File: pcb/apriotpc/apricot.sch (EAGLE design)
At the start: 16 parts, among them J2 ATX24RH

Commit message: added grounding blade and exposed screw pad, added psw blade
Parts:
- added U$5, U$6: M3_MOUNTING_HOLE, apricot:M3_MOUNTING_HOLE
- added U$7: 6MM_BLADE, apricot:6MM_BLADE
- JP1: device pinhead:PINHD-1X2/90 -> pinhead:PINHD-1X2
- U$1, U$3: value M3_MOUNTING_HOLE -> 6MM_BLADE; device a:M3_MOUNTING_HOLE -> apricot:6MM_BLADE
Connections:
- net GND: now also JP1.1, U$3.P$1, U$3.P$2, U$5.P$1, U$5.P$2, U$6.P$1, U$6.P$2, U$7.P$1, U$7.P$2; no longer JP1.2
- net N$1: now also JP1.2, U$1.P$1, U$1.P$2; no longer JP1.1
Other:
- moved on the sheet: JP1
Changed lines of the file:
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@@
 <part name="GND4" library="supply1" library_urn="urn:adsk.eagle:library:371" deviceset="GND" device=""/>
 <part name="JP3" library="appleii" deviceset="4PIN_FAN" device=""/>
-<part name="U$1" library="a" deviceset="M3_MOUNTING_HOLE" device=""/>
-<part name="U$3" library="a" deviceset="M3_MOUNTING_HOLE" device=""/>
 <part name="GND1" library="supply1" library_urn="urn:adsk.eagle:library:371" deviceset="GND" device=""/>
 <part name="C2" library="capacitor-wima" library_urn="urn:adsk.eagle:library:116" deviceset="C" device="5/2.5" package3d_urn="urn:adsk.eagle:package:5426/1"/>
@@
 <part name="GND9" library="supply1" library_urn="urn:adsk.eagle:library:371" deviceset="GND" device=""/>
 <part name="U$4" library="396_conn" deviceset="VH396" device=""/>
-<part name="JP1" library="pinhead" library_urn="urn:adsk.eagle:library:325" deviceset="PINHD-1X2" device="/90" package3d_urn="urn:adsk.eagle:package:22437/2"/>
+<part name="JP1" library="pinhead" library_urn="urn:adsk.eagle:library:325" deviceset="PINHD-1X2" device="" package3d_urn="urn:adsk.eagle:package:22435/2"/>
 <part name="P+1" library="supply1" library_urn="urn:adsk.eagle:library:371" deviceset="+12V" device=""/>
 <part name="P+4" library="supply1" library_urn="urn:adsk.eagle:library:371" deviceset="+5V" device=""/>
@@
 <part name="GND13" library="supply1" library_urn="urn:adsk.eagle:library:371" deviceset="GND" device=""/>
 <part name="P+13" library="supply1" library_urn="urn:adsk.eagle:library:371" deviceset="+5V" device=""/>
+<part name="U$5" library="apricot" deviceset="M3_MOUNTING_HOLE" device=""/>
+<part name="U$6" library="apricot" deviceset="M3_MOUNTING_HOLE" device=""/>
+<part name="GND6" library="supply1" library_urn="urn:adsk.eagle:library:371" deviceset="GND" device=""/>
+<part name="U$1" library="apricot" deviceset="6MM_BLADE" device=""/>
+<part name="U$3" library="apricot" deviceset="6MM_BLADE" device=""/>
+<part name="U$7" library="apricot" deviceset="6MM_BLADE" device=""/>
+<part name="GND14" library="supply1" library_urn="urn:adsk.eagle:library:371" deviceset="GND" device=""/>
 </parts>
 <sheets>
@@
 </instance>
 <instance part="JP3" gate="A" x="-55.88" y="132.08" smashed="yes"/>
-<instance part="U$1" gate="G$1" x="-66.04" y="170.18" smashed="yes"/>
-<instance part="U$3" gate="G$1" x="-66.04" y="160.02" smashed="yes"/>
-<instance part="GND1" gate="1" x="121.92" y="154.94" smashed="yes">
-<attribute name="VALUE" x="119.38" y="152.4" size="1.778" layer="96"/>
+<instance part="GND1" gate="1" x="139.7" y="162.56" smashed="yes">
+<attribute name="VALUE" x="137.16" y="160.02" size="1.778" layer="96"/>
 </instance>
 <instance part="C2" gate="G$1" x="152.4" y="149.86" smashed="yes">
@@
 </instance>
 <instance part="U$4" gate="G$1" x="27.94" y="132.08" smashed="yes" rot="R180"/>
-<instance part="JP1" gate="G$1" x="132.08" y="160.02" smashed="yes">
-<attribute name="NAME" x="125.73" y="165.735" size="1.778" layer="95"/>
-<attribute name="VALUE" x="125.73" y="154.94" size="1.778" layer="96"/>
+<instance part="JP1" gate="G$1" x="132.08" y="162.56" smashed="yes">
+<attribute name="NAME" x="125.73" y="168.275" size="1.778" layer="95"/>
+<attribute name="VALUE" x="125.73" y="157.48" size="1.778" layer="96"/>
 </instance>
 <instance part="P+1" gate="1" x="43.18" y="142.24" smashed="yes" rot="MR0">
@@
 <instance part="P+13" gate="1" x="71.12" y="101.6" smashed="yes">
 <attribute name="VALUE" x="68.58" y="96.52" size="1.778" layer="96" rot="R90"/>
+</instance>
+<instance part="U$5" gate="G$1" x="-35.56" y="187.96" smashed="yes"/>
+<instance part="U$6" gate="G$1" x="-35.56" y="170.18" smashed="yes"/>
+<instance part="GND6" gate="1" x="-7.62" y="165.1" smashed="yes">
+<attribute name="VALUE" x="-10.16" y="162.56" size="1.778" layer="96"/>
+</instance>
+<instance part="U$1" gate="G$1" x="127" y="132.08" smashed="yes" rot="R90"/>
+<instance part="U$3" gate="G$1" x="190.5" y="119.38" smashed="yes"/>
+<instance part="U$7" gate="G$1" x="190.5" y="129.54" smashed="yes"/>
+<instance part="GND14" gate="1" x="218.44" y="114.3" smashed="yes">
+<attribute name="VALUE" x="215.9" y="111.76" size="1.778" layer="96"/>
 </instance>
 </instances>
@@
 </segment>
 <segment>
-<pinref part="JP1" gate="G$1" pin="2"/>
-<pinref part="GND1" gate="1" pin="GND"/>
-<wire x1="129.54" y1="160.02" x2="121.92" y2="160.02" width="0.1524" layer="91"/>
-<wire x1="121.92" y1="160.02" x2="121.92" y2="157.48" width="0.1524" layer="91"/>
-</segment>
-<segment>
 <pinref part="U$4" gate="G$1" pin="P$2"/>
 <pinref part="GND3" gate="1" pin="GND"/>
@@
 <pinref part="C8" gate="G$1" pin="2"/>
 <pinref part="GND13" gate="1" pin="GND"/>
+</segment>
+<segment>
+<pinref part="U$5" gate="G$1" pin="P$1"/>
+<pinref part="GND6" gate="1" pin="GND"/>
+<wire x1="-12.7" y1="193.04" x2="-7.62" y2="193.04" width="0.1524" layer="91"/>
+<wire x1="-7.62" y1="193.04" x2="-7.62" y2="185.42" width="0.1524" layer="91"/>
+<pinref part="U$5" gate="G$1" pin="P$2"/>
+<wire x1="-7.62" y1="185.42" x2="-7.62" y2="175.26" width="0.1524" layer="91"/>
+<wire x1="-7.62" y1="175.26" x2="-7.62" y2="167.64" width="0.1524" layer="91"/>
+<wire x1="-12.7" y1="185.42" x2="-7.62" y2="185.42" width="0.1524" layer="91"/>
+<junction x="-7.62" y="185.42"/>
+<pinref part="U$6" gate="G$1" pin="P$1"/>
+<wire x1="-12.7" y1="175.26" x2="-7.62" y2="175.26" width="0.1524" layer="91"/>
+<junction x="-7.62" y="175.26"/>
+<pinref part="U$6" gate="G$1" pin="P$2"/>
+<wire x1="-12.7" y1="167.64" x2="-7.62" y2="167.64" width="0.1524" layer="91"/>
+<junction x="-7.62" y="167.64"/>
+</segment>
+<segment>
+<pinref part="JP1" gate="G$1" pin="1"/>
+<pinref part="GND1" gate="1" pin="GND"/>
+<wire x1="129.54" y1="165.1" x2="139.7" y2="165.1" width="0.1524" layer="91"/>
+</segment>
+<segment>
+<pinref part="U$7" gate="G$1" pin="P$1"/>
+<pinref part="GND14" gate="1" pin="GND"/>
+<wire x1="208.28" y1="132.08" x2="218.44" y2="132.08" width="0.1524" layer="91"/>
+<wire x1="218.44" y1="132.08" x2="218.44" y2="127" width="0.1524" layer="91"/>
+<pinref part="U$3" gate="G$1" pin="P$2"/>
+<wire x1="218.44" y1="127" x2="218.44" y2="121.92" width="0.1524" layer="91"/>
+<wire x1="218.44" y1="121.92" x2="218.44" y2="116.84" width="0.1524" layer="91"/>
+<wire x1="208.28" y1="116.84" x2="218.44" y2="116.84" width="0.1524" layer="91"/>
+<junction x="218.44" y="116.84"/>
+<pinref part="U$3" gate="G$1" pin="P$1"/>
+<wire x1="208.28" y1="121.92" x2="218.44" y2="121.92" width="0.1524" layer="91"/>
+<junction x="218.44" y="121.92"/>
+<pinref part="U$7" gate="G$1" pin="P$2"/>
+<wire x1="208.28" y1="127" x2="218.44" y2="127" width="0.1524" layer="91"/>
+<junction x="218.44" y="127"/>
 </segment>
 </net>
@@
 </segment>
 </net>
-<net name="N$1" class="0">
-<segment>
-<pinref part="J2" gate="G$1" pin="PS_ON"/>
-<wire x1="109.22" y1="162.56" x2="129.54" y2="162.56" width="0.1524" layer="91"/>
-<pinref part="JP1" gate="G$1" pin="1"/>
-</segment>
-</net>
 <net name="N$2" class="0">
 <segment>
@@
 </segment>
 </net>
+<net name="N$1" class="0">
+<segment>
+<pinref part="J2" gate="G$1" pin="PS_ON"/>
+<pinref part="JP1" gate="G$1" pin="2"/>
+<wire x1="109.22" y1="162.56" x2="124.46" y2="162.56" width="0.1524" layer="91"/>
+<pinref part="U$1" gate="G$1" pin="P$1"/>
+<wire x1="124.46" y1="162.56" x2="129.54" y2="162.56" width="0.1524" layer="91"/>
+<wire x1="124.46" y1="149.86" x2="124.46" y2="162.56" width="0.1524" layer="91"/>
+<junction x="124.46" y="162.56"/>
+<pinref part="U$1" gate="G$1" pin="P$2"/>
+<wire x1="129.54" y1="149.86" x2="124.46" y2="149.86" width="0.1524" layer="91"/>
+<junction x="124.46" y="149.86"/>
+</segment>
+</net>

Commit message: adjust apricot pc resistors
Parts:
- added C10, C12: 100nF, clock:CAP0805
- added C11, C9: (no value), adafruit:CPOL-USE5-10.5
- C3, C7: value (none) -> 100nF; device capacitor-wima:C5/2.5 -> clock:CAP0805
- C4: device capacitor-wima:C5/2.5 -> adafruit:CPOL-USE5-10.5
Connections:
- net +12V: now also C10.2, C3.2, C4.+, C9.+; no longer C3.1, C4.1
- net +5V: now also C11.+, C12.2, C7.2; no longer C7.1
- net GND: now also C10.1, C11.-, C12.1, C3.1, C4.-, C7.1, C9.-; no longer C3.2, C4.2, C7.2
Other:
- moved on the sheet: C3, C7

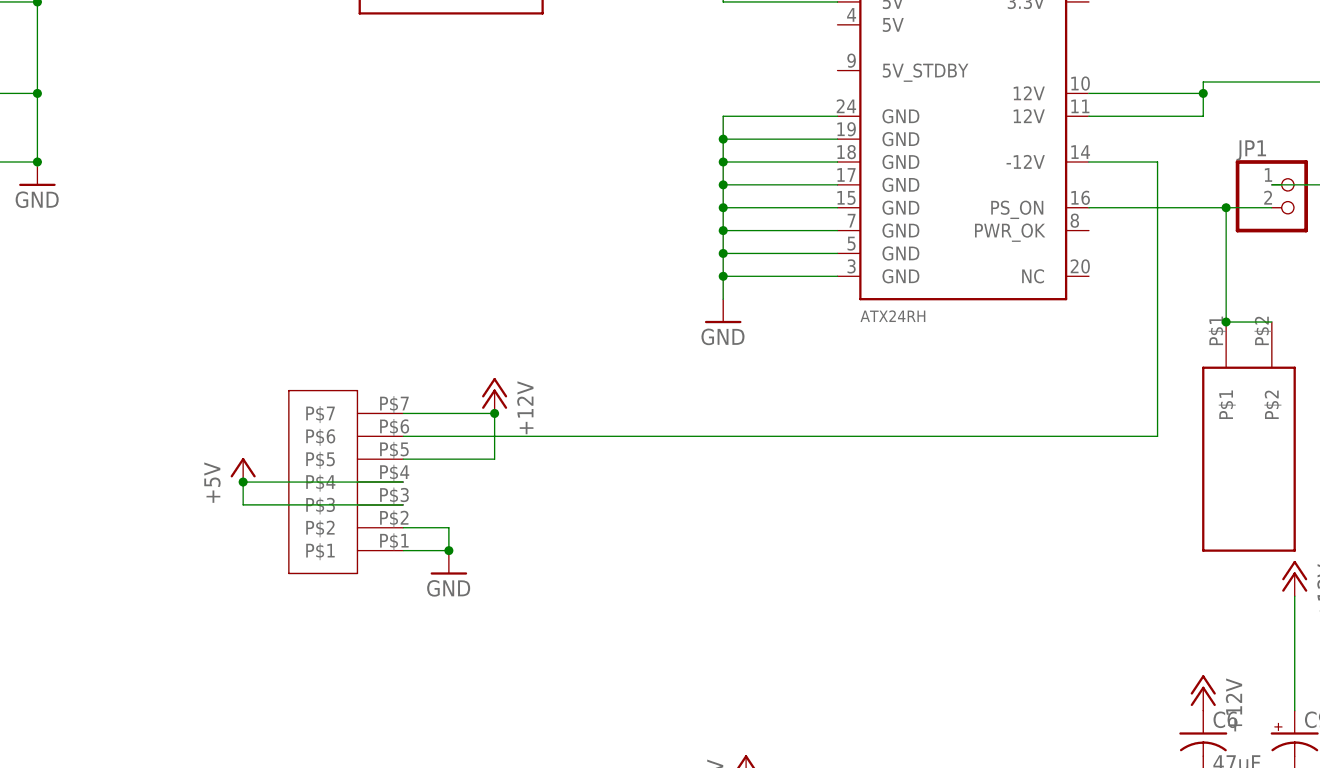
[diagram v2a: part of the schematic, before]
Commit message: fixed connector oritation
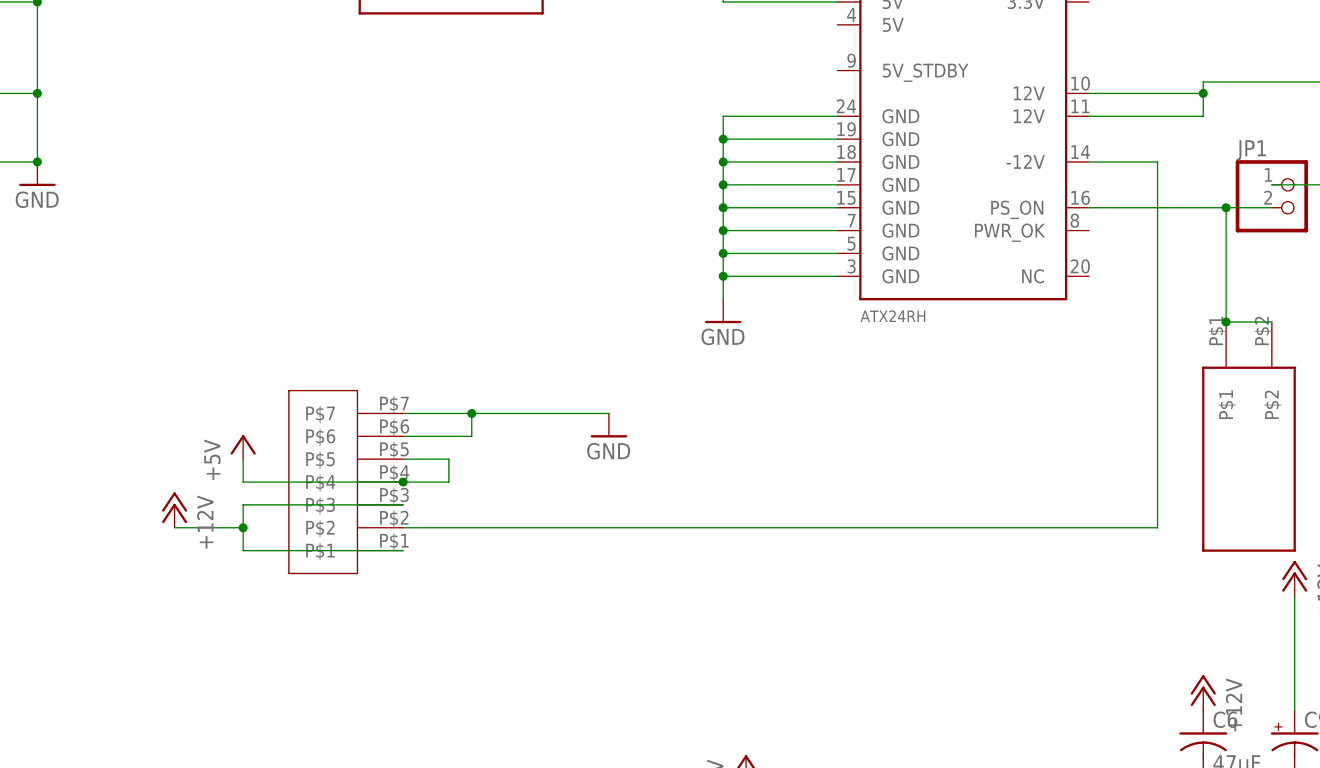
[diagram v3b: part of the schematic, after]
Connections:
- net +12V: now also U$4.P$1, U$4.P$3; no longer U$4.P$5, U$4.P$7
- net +5V: now also U$4.P$5; no longer U$4.P$3
- net GND: now also U$4.P$6, U$4.P$7; no longer U$4.P$1, U$4.P$2
- net N$2: now also U$4.P$2; no longer U$4.P$6
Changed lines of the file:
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@@
 <attribute name="VALUE" x="125.73" y="157.48" size="1.778" layer="96"/>
 </instance>
-<instance part="P+1" gate="1" x="43.18" y="142.24" smashed="yes" rot="MR0">
-<attribute name="VALUE" x="45.72" y="137.16" size="1.778" layer="96" rot="MR90"/>
-</instance>
-<instance part="P+4" gate="1" x="15.24" y="134.62" smashed="yes">
-<attribute name="VALUE" x="12.7" y="129.54" size="1.778" layer="96" rot="R90"/>
-</instance>
-<instance part="GND3" gate="1" x="38.1" y="121.92" smashed="yes">
-<attribute name="VALUE" x="35.56" y="119.38" size="1.778" layer="96"/>
+<instance part="P+1" gate="1" x="7.62" y="129.54" smashed="yes" rot="MR0">
+<attribute name="VALUE" x="10.16" y="124.46" size="1.778" layer="96" rot="MR90"/>
+</instance>
+<instance part="P+4" gate="1" x="15.24" y="137.16" smashed="yes">
+<attribute name="VALUE" x="12.7" y="132.08" size="1.778" layer="96" rot="R90"/>
+</instance>
+<instance part="GND3" gate="1" x="55.88" y="137.16" smashed="yes">
+<attribute name="VALUE" x="53.34" y="134.62" size="1.778" layer="96"/>
 </instance>
 <instance part="GND5" gate="1" x="165.1" y="129.54" smashed="yes">
@@
 </segment>
 <segment>
-<pinref part="U$4" gate="G$1" pin="P$2"/>
-<pinref part="GND3" gate="1" pin="GND"/>
-<wire x1="33.02" y1="127" x2="38.1" y2="127" width="0.1524" layer="91"/>
-<wire x1="38.1" y1="127" x2="38.1" y2="124.46" width="0.1524" layer="91"/>
-<pinref part="U$4" gate="G$1" pin="P$1"/>
-<wire x1="33.02" y1="124.46" x2="38.1" y2="124.46" width="0.1524" layer="91"/>
-<junction x="38.1" y="124.46"/>
-</segment>
-<segment>
 <pinref part="GND7" gate="1" pin="GND"/>
 <wire x1="132.08" y1="81.28" x2="132.08" y2="99.06" width="0.1524" layer="91"/>
@@
 <wire x1="73.66" y1="66.04" x2="83.82" y2="66.04" width="0.1524" layer="91"/>
 <junction x="73.66" y="66.04"/>
+</segment>
+<segment>
+<pinref part="U$4" gate="G$1" pin="P$7"/>
+<pinref part="GND3" gate="1" pin="GND"/>
+<wire x1="33.02" y1="139.7" x2="40.64" y2="139.7" width="0.1524" layer="91"/>
+<pinref part="U$4" gate="G$1" pin="P$6"/>
+<wire x1="40.64" y1="139.7" x2="55.88" y2="139.7" width="0.1524" layer="91"/>
+<wire x1="33.02" y1="137.16" x2="40.64" y2="137.16" width="0.1524" layer="91"/>
+<wire x1="40.64" y1="137.16" x2="40.64" y2="139.7" width="0.1524" layer="91"/>
+<junction x="40.64" y="139.7"/>
 </segment>
 </net>
@@
 </segment>
 <segment>
-<pinref part="P+4" gate="1" pin="+5V"/>
-<pinref part="U$4" gate="G$1" pin="P$4"/>
-<wire x1="15.24" y1="132.08" x2="33.02" y2="132.08" width="0.1524" layer="91"/>
-<pinref part="U$4" gate="G$1" pin="P$3"/>
-<wire x1="33.02" y1="129.54" x2="15.24" y2="129.54" width="0.1524" layer="91"/>
-<wire x1="15.24" y1="129.54" x2="15.24" y2="132.08" width="0.1524" layer="91"/>
-<junction x="15.24" y="132.08"/>
-</segment>
-<segment>
 <pinref part="C8" gate="G$1" pin="1"/>
 <pinref part="P+13" gate="1" pin="+5V"/>
@@
 <wire x1="73.66" y1="73.66" x2="83.82" y2="73.66" width="0.1524" layer="91"/>
 <junction x="73.66" y="73.66"/>
+</segment>
+<segment>
+<pinref part="U$4" gate="G$1" pin="P$5"/>
+<wire x1="33.02" y1="134.62" x2="38.1" y2="134.62" width="0.1524" layer="91"/>
+<wire x1="38.1" y1="134.62" x2="38.1" y2="132.08" width="0.1524" layer="91"/>
+<pinref part="U$4" gate="G$1" pin="P$4"/>
+<wire x1="38.1" y1="132.08" x2="33.02" y2="132.08" width="0.1524" layer="91"/>
+<pinref part="P+4" gate="1" pin="+5V"/>
+<wire x1="33.02" y1="132.08" x2="15.24" y2="132.08" width="0.1524" layer="91"/>
+<wire x1="15.24" y1="132.08" x2="15.24" y2="134.62" width="0.1524" layer="91"/>
+<junction x="33.02" y="132.08"/>
 </segment>
 </net>
@@
 </segment>
 <segment>
-<pinref part="U$4" gate="G$1" pin="P$7"/>
-<pinref part="P+1" gate="1" pin="+12V"/>
-<wire x1="33.02" y1="139.7" x2="43.18" y2="139.7" width="0.1524" layer="91"/>
-<pinref part="U$4" gate="G$1" pin="P$5"/>
-<wire x1="33.02" y1="134.62" x2="43.18" y2="134.62" width="0.1524" layer="91"/>
-<wire x1="43.18" y1="134.62" x2="43.18" y2="139.7" width="0.1524" layer="91"/>
-<junction x="43.18" y="139.7"/>
-</segment>
-<segment>
 <pinref part="C5" gate="G$1" pin="1"/>
 <pinref part="P+6" gate="1" pin="+12V"/>
@@
 <junction x="180.34" y="152.4"/>
 </segment>
+<segment>
+<pinref part="P+1" gate="1" pin="+12V"/>
+<wire x1="7.62" y1="127" x2="15.24" y2="127" width="0.1524" layer="91"/>
+<wire x1="15.24" y1="127" x2="15.24" y2="124.46" width="0.1524" layer="91"/>
+<pinref part="U$4" gate="G$1" pin="P$1"/>
+<wire x1="15.24" y1="124.46" x2="33.02" y2="124.46" width="0.1524" layer="91"/>
+<pinref part="U$4" gate="G$1" pin="P$3"/>
+<wire x1="33.02" y1="129.54" x2="15.24" y2="129.54" width="0.1524" layer="91"/>
+<wire x1="15.24" y1="129.54" x2="15.24" y2="127" width="0.1524" layer="91"/>
+<junction x="15.24" y="127"/>
+</segment>
 </net>
 <net name="N$2" class="0">
 <segment>
-<pinref part="U$4" gate="G$1" pin="P$6"/>
-<wire x1="33.02" y1="137.16" x2="116.84" y2="137.16" width="0.1524" layer="91"/>
-<wire x1="116.84" y1="137.16" x2="116.84" y2="167.64" width="0.1524" layer="91"/>
+<wire x1="116.84" y1="127" x2="116.84" y2="167.64" width="0.1524" layer="91"/>
 <pinref part="J2" gate="G$1" pin="-12V"/>
 <wire x1="116.84" y1="167.64" x2="109.22" y2="167.64" width="0.1524" layer="91"/>
-</segment>
-</net>
+<pinref part="U$4" gate="G$1" pin="P$2"/>
+<wire x1="116.84" y1="127" x2="33.02" y2="127" width="0.1524" layer="91"/>
+</segment>
+</net>

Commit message: changed to smaller diameter caps
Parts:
- added C13: (no value), capacitor-wima:C5/2.5
- C11, C4, C9: device adafruit:CPOL-USE5-10.5 -> adafruit_changed:CPOL-USE3.5-8
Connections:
- net +12V: now also C13.1
- net GND: now also C13.2
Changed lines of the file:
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@@
 <part name="U$7" library="apricot" deviceset="6MM_BLADE" device=""/>
 <part name="GND14" library="supply1" library_urn="urn:adsk.eagle:library:371" deviceset="GND" device=""/>
-<part name="C9" library="adafruit" deviceset="CPOL-US" device="E5-10.5"/>
-<part name="C4" library="adafruit" deviceset="CPOL-US" device="E5-10.5"/>
+<part name="C9" library="adafruit_changed" deviceset="CPOL-US" device="E3.5-8"/>
+<part name="C4" library="adafruit_changed" deviceset="CPOL-US" device="E3.5-8"/>
 <part name="C3" library="clock" deviceset="CAP" device="0805" value="100nF"/>
 <part name="C10" library="clock" deviceset="CAP" device="0805" value="100nF"/>
-<part name="C11" library="adafruit" deviceset="CPOL-US" device="E5-10.5"/>
+<part name="C11" library="adafruit_changed" deviceset="CPOL-US" device="E3.5-8"/>
 <part name="C7" library="clock" deviceset="CAP" device="0805" value="100nF"/>
 <part name="C12" library="clock" deviceset="CAP" device="0805" value="100nF"/>
 <part name="P+9" library="supply1" library_urn="urn:adsk.eagle:library:371" deviceset="+5V" device=""/>
 <part name="GND15" library="supply1" library_urn="urn:adsk.eagle:library:371" deviceset="GND" device=""/>
+<part name="C13" library="capacitor-wima" library_urn="urn:adsk.eagle:library:116" deviceset="C" device="5/2.5" package3d_urn="urn:adsk.eagle:package:5426/1"/>
+<part name="GND16" library="supply1" library_urn="urn:adsk.eagle:library:371" deviceset="GND" device=""/>
+<part name="P+14" library="supply1" library_urn="urn:adsk.eagle:library:371" deviceset="+12V" device=""/>
 </parts>
 <sheets>
@@
 <instance part="GND15" gate="1" x="73.66" y="60.96" smashed="yes">
 <attribute name="VALUE" x="71.12" y="58.42" size="1.778" layer="96"/>
+</instance>
+<instance part="C13" gate="G$1" x="160.02" y="104.14" smashed="yes">
+<attribute name="NAME" x="161.544" y="104.521" size="1.778" layer="95"/>
+<attribute name="VALUE" x="161.544" y="99.441" size="1.778" layer="96"/>
+</instance>
+<instance part="GND16" gate="1" x="160.02" y="96.52" smashed="yes">
+<attribute name="VALUE" x="157.48" y="93.98" size="1.778" layer="96"/>
+</instance>
+<instance part="P+14" gate="1" x="160.02" y="116.84" smashed="yes" rot="MR0">
+<attribute name="VALUE" x="162.56" y="111.76" size="1.778" layer="96" rot="MR90"/>
 </instance>
 </instances>
@@
 <junction x="40.64" y="139.7"/>
 </segment>
+<segment>
+<pinref part="C13" gate="G$1" pin="2"/>
+<pinref part="GND16" gate="1" pin="GND"/>
+</segment>
 </net>
 <net name="N$6" class="0">
@@
 <junction x="15.24" y="127"/>
 </segment>
+<segment>
+<pinref part="C13" gate="G$1" pin="1"/>
+<pinref part="P+14" gate="1" pin="+12V"/>
+<wire x1="160.02" y1="114.3" x2="160.02" y2="106.68" width="0.1524" layer="91"/>
+</segment>
 </net>
